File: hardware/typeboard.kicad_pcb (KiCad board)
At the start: 4 copper layers, 288.8 x 97.2 mm, 136 parts

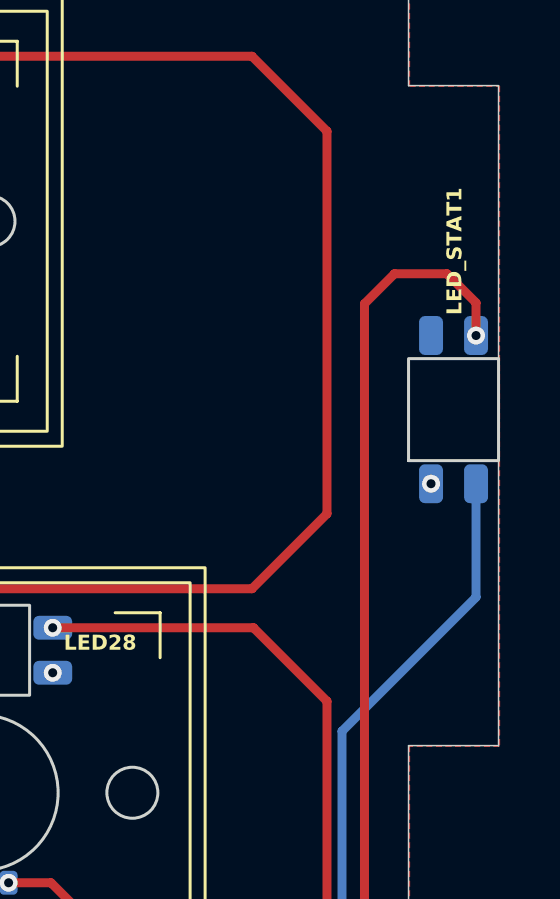
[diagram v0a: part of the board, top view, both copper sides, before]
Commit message: :recycle: refine layers
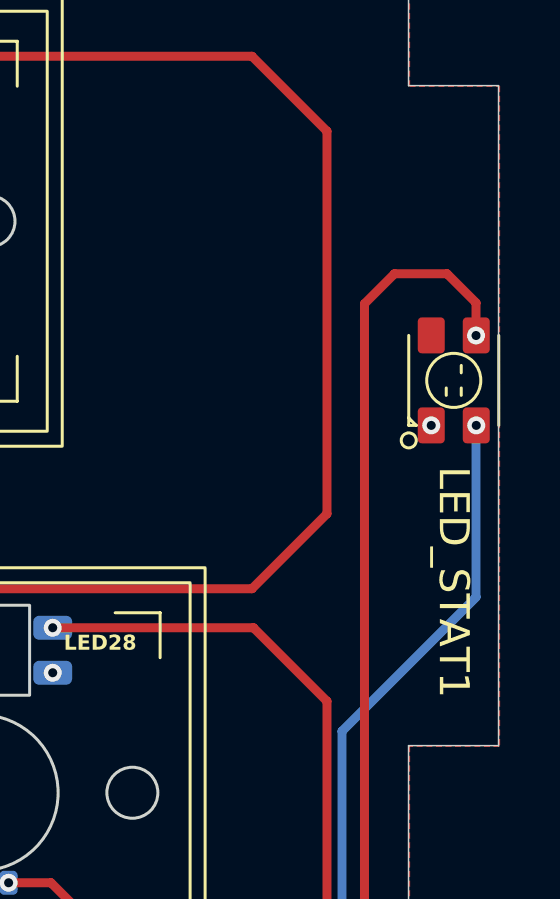
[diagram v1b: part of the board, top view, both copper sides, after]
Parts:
- LED_STAT1: footprint KeysDock:XL-6028RGBW-WS2812B -> KeysDock:XL-3528RGBW-WS2812B
- moved LED_STAT1 0.96 mm to (345.2, 55.3), turned to -90 degrees
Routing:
- net Net-(LED64-DO): track 67.5 -> 69.5 mm, vias 0 -> 1
